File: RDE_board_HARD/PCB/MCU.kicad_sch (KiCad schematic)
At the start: 19 parts, among them J2 TC2030, J3 Conn_01x02_Pin, U2 STM32G431CBTx, U6 FM24C64B, Y1 3225-25M-SR

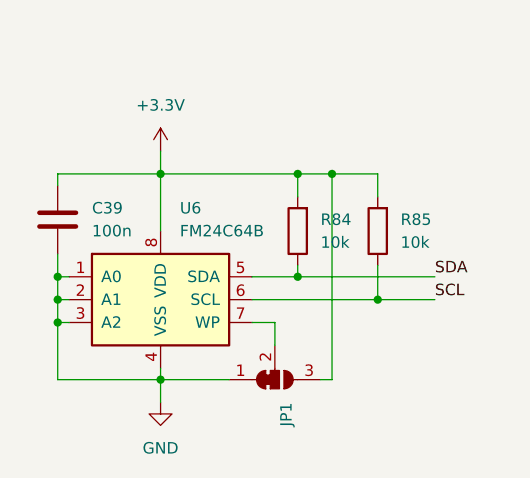
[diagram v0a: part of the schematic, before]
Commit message: Added i2c for backplane config, testpoints. File organization
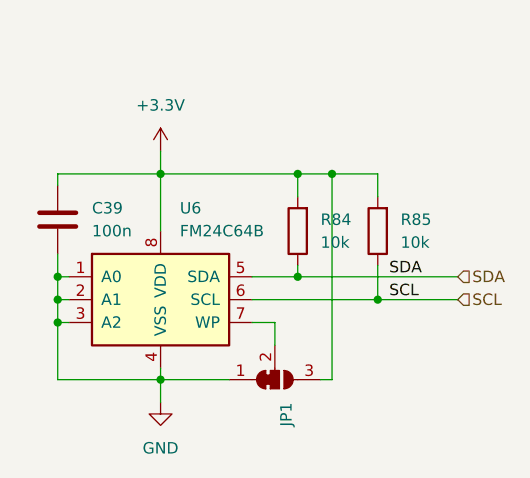
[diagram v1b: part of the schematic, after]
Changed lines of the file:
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@@
-	(wire
-		(pts
-			(xy 259.08 138.43) (xy 259.08 134.62)
-		)
-		(stroke
-			(width 0)
-			(type default)
-		)
-	)
 	(wire
 		(pts
@@
 	(wire
 		(pts
-			(xy 250.19 135.89) (xy 265.43 135.89)
+			(xy 250.19 135.89) (xy 267.97 135.89)
 		)
 		(stroke
@@
 	(wire
 		(pts
-			(xy 259.08 138.43) (xy 265.43 138.43)
-		)
-		(stroke
-			(width 0)
-			(type default)
-		)
-	)
-	(wire
-		(pts
 			(xy 245.11 140.97) (xy 247.65 140.97)
 		)
@@
 	(wire
 		(pts
+			(xy 259.08 134.62) (xy 259.08 138.43)
+		)
+		(stroke
+			(width 0)
+			(type default)
+		)
+	)
+	(wire
+		(pts
 			(xy 140.97 54.61) (xy 143.51 54.61)
 		)
@@
 		(pts
 			(xy 109.22 100.33) (xy 123.19 100.33)
+		)
+		(stroke
+			(width 0)
+			(type default)
+		)
+	)
+	(wire
+		(pts
+			(xy 259.08 138.43) (xy 267.97 138.43)
 		)
 		(stroke
@@
 	)
 	(label "SDA"
-		(at 265.43 135.89 0)
+		(at 260.35 135.89 0)
 		(effects
 			(font
@@
 	)
 	(label "SCL"
-		(at 265.43 138.43 0)
+		(at 260.35 138.43 0)
 		(effects
 			(font
@@
 		)
 	)
+	(hierarchical_label "SDA"
+		(shape input)
+		(at 267.97 135.89 0)
+		(effects
+			(font
+				(size 1.27 1.27)
+			)
+			(justify left)
+		)
+	)
+	(hierarchical_label "SCL"
+		(shape input)
+		(at 267.97 138.43 0)
+		(effects
+			(font
+				(size 1.27 1.27)
+			)
+			(justify left)
+		)
+	)
